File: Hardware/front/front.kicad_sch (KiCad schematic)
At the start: 17 parts, among them J101 Conn_02x10_Odd_Even, J102 Conn_02x08_Odd_Even, U101 XRA1203, U102 AT24CS32-SSHM, U103 PCA9955B

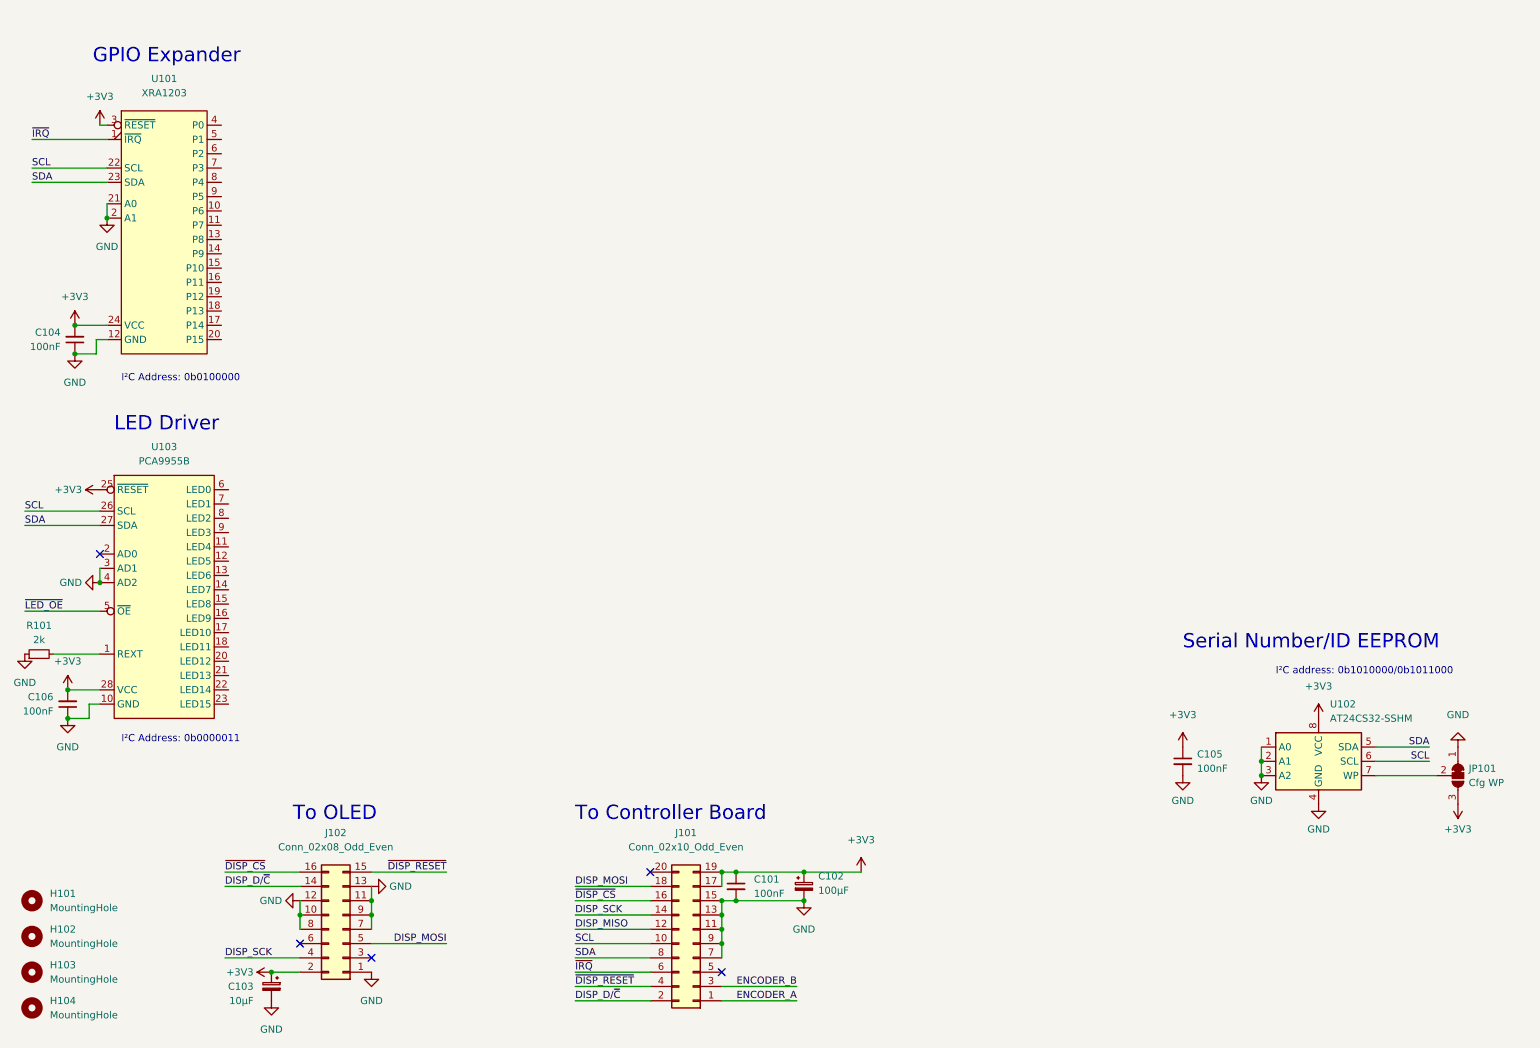
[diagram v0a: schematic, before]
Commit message: Finished front panel board
- Added all the switches/encoders required for the front panel, as well
  as the indicators. They are in (roughly? hopefully lol) the right
  places for the current front panel design.

  The PCB shall be mounted on 4x 8mm standoffs with M2 screws.
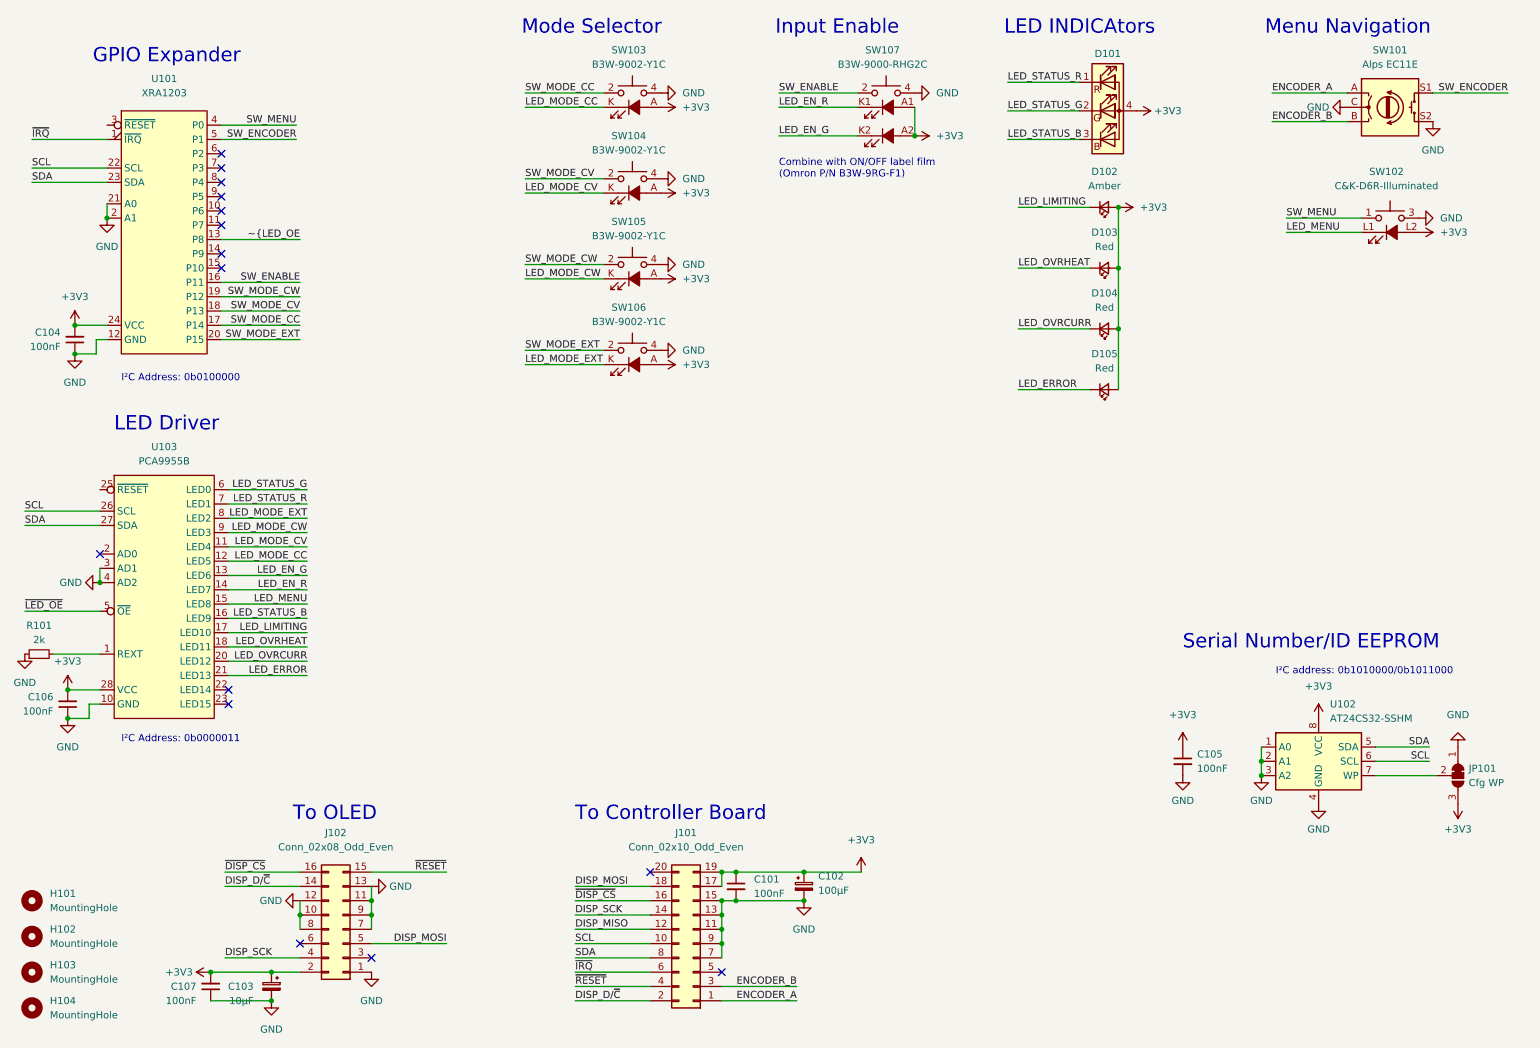
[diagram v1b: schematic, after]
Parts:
- added C107: 100nF, Capacitor_SMD:C_0805_2012Metric_Pad1.18x1.45mm_HandSolder, symbol Device:C_Small
- added D101: LED_RGBA, LED_SMD:LED_RGB_1210, symbol Device:LED_RGBA
- added D102: Amber, LED_SMD:LED_1206_3216Metric_Pad1.42x1.75mm_HandSolder, symbol Device:LED_Small
- added D103, D104, D105: Red, LED_SMD:LED_1206_3216Metric_Pad1.42x1.75mm_HandSolder, symbol Device:LED_Small
- added SW101: Alps EC11E, Rotary_Encoder:RotaryEncoder_Alps_EC11E-Switch_Vertical_H20mm, symbol Device:RotaryEncoder_Switch
- added SW102: C&K-D6R-Illuminated, programmable-load:C&K-D6R-LED, symbol programmable-load:C&K-D6R-Illuminated
- added SW103, SW104, SW105, SW106: B3W-9002-Y1C, programmable-load:Omron-B3W-90XX-X1X, symbol programmable-load:B3W-900X-X1X
- added SW107: B3W-9000-RHG2C, programmable-load:Omron-B3W-90XX-X2X, symbol programmable-load:B3W-900X-X2X
- H101, H102, H103, H104, JP101: now left out of the parts list
- J101: MPN 20021221-00020C1LF -> 20021221-00020C1LF, 20021121-00020C1LF
- J102: footprint Connector_PinHeader_2.54mm:PinHeader_2x08_P2.54mm_Vertical -> Connector_PinHeader_2.54mm:PinHeader_2x08_P2.54mm_Vertical_SMD; MPN (none) -> 10129383-916001ALF
- U101: MPN (none) -> XRA1203IG24TR-F
- U102: MPN (none) -> AT24CS32-SSHM
- U103: MPN (none) -> PCA9955BTWJ
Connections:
- net +3V3: now also C107.2, D101.4 (A), D102.2 (A), D103.2 (A), D104.2 (A), D105.2 (A), SW102.L2, SW103.A, SW104.A, SW105.A, SW106.A, SW107.A1, SW107.A2; no longer U101.3 (~{RESET}), U103.25 (~{RESET})
- net ENCODER_A: now also SW101.A
- net ENCODER_B: now also SW101.B
- net GND: now also C107.1, SW101.C, SW101.S2, SW102.3 (2), SW102.4 (2), SW103.3, SW103.4, SW104.3, SW104.4, SW105.3, SW105.4, SW106.3, SW106.4, SW107.3, SW107.4
- net ~{LED_OE: now reaches U101.13 (P8)
- net SW_ENABLE: now reaches U101.16 (P11)
- net SW_ENABLE: now also SW107.1, SW107.2
- net SW_MODE_CC: now reaches U101.17 (P14)
- net SW_MODE_CC: now also SW103.1, SW103.2
- net SW_MODE_CV: now reaches U101.18 (P13)
- net SW_MODE_CV: now also SW104.1, SW104.2
- net SW_MODE_CW: now reaches U101.19 (P12)
- net SW_MODE_CW: now also SW105.1, SW105.2
- net SW_MODE_EXT: now reaches U101.20 (P15)
- net SW_MODE_EXT: now also SW106.1, SW106.2
- net SW_MENU: now reaches U101.4 (P0)
- net SW_MENU: now also SW102.1, SW102.2 (1)
- net SW_ENCODER: now reaches U101.5 (P1)
- net SW_ENCODER: now also SW101.S1
- net LED_MODE_CV: now reaches U103.11 (LED4)
- net LED_MODE_CV: now also SW104.K
- net LED_MODE_CC: now reaches U103.12 (LED5)
- net LED_MODE_CC: now also SW103.K
- net LED_EN_G: now reaches U103.13 (LED6)
- net LED_EN_G: now also SW107.K2 (K)
- net LED_EN_R: now reaches U103.14 (LED7)
- net LED_EN_R: now also SW107.K1 (K)
- net LED_MENU: now reaches U103.15 (LED8)
- net LED_MENU: now also SW102.L1
- net LED_STATUS_B: now reaches U103.16 (LED9)
- net LED_STATUS_B: now also D101.3 (BK)
- net LED_LIMITING: now reaches U103.17 (LED10)
- net LED_LIMITING: now also D102.1 (K)
- net LED_OVRHEAT: now reaches U103.18 (LED11)
- net LED_OVRHEAT: now also D103.1 (K)
- net LED_OVRCURR: now reaches U103.20 (LED12)
- net LED_OVRCURR: now also D104.1 (K)
- net LED_ERROR: now reaches U103.21 (LED13)
- net LED_ERROR: now also D105.1 (K)
- net LED_STATUS_G: now reaches U103.6 (LED0)
- net LED_STATUS_G: now also D101.2 (GK)
- net LED_STATUS_R: now reaches U103.7 (LED1)
- net LED_STATUS_R: now also D101.1 (RK)
- net LED_MODE_EXT: now reaches U103.8 (LED2)
- net LED_MODE_EXT: now also SW106.K
- net LED_MODE_CW: now reaches U103.9 (LED3)
- net LED_MODE_CW: now also SW105.K
- net ~{DISP_RESET} renamed ~{RESET}
- no-connect marks 5 -> 15
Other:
- note added: "Combine with ON/OFF label film (Omron P/N B3W-9RG-F1)"
- note added: "Input Enable"
- note added: "LED INDICAtors"
- note added: "Menu Navigation"
- note added: "Mode Selector"

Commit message: Front panel layout tweaks
- Made space for a ~38mm diameter knob on the rotary encoder, by moving
  the indicators and menu button somewhat.
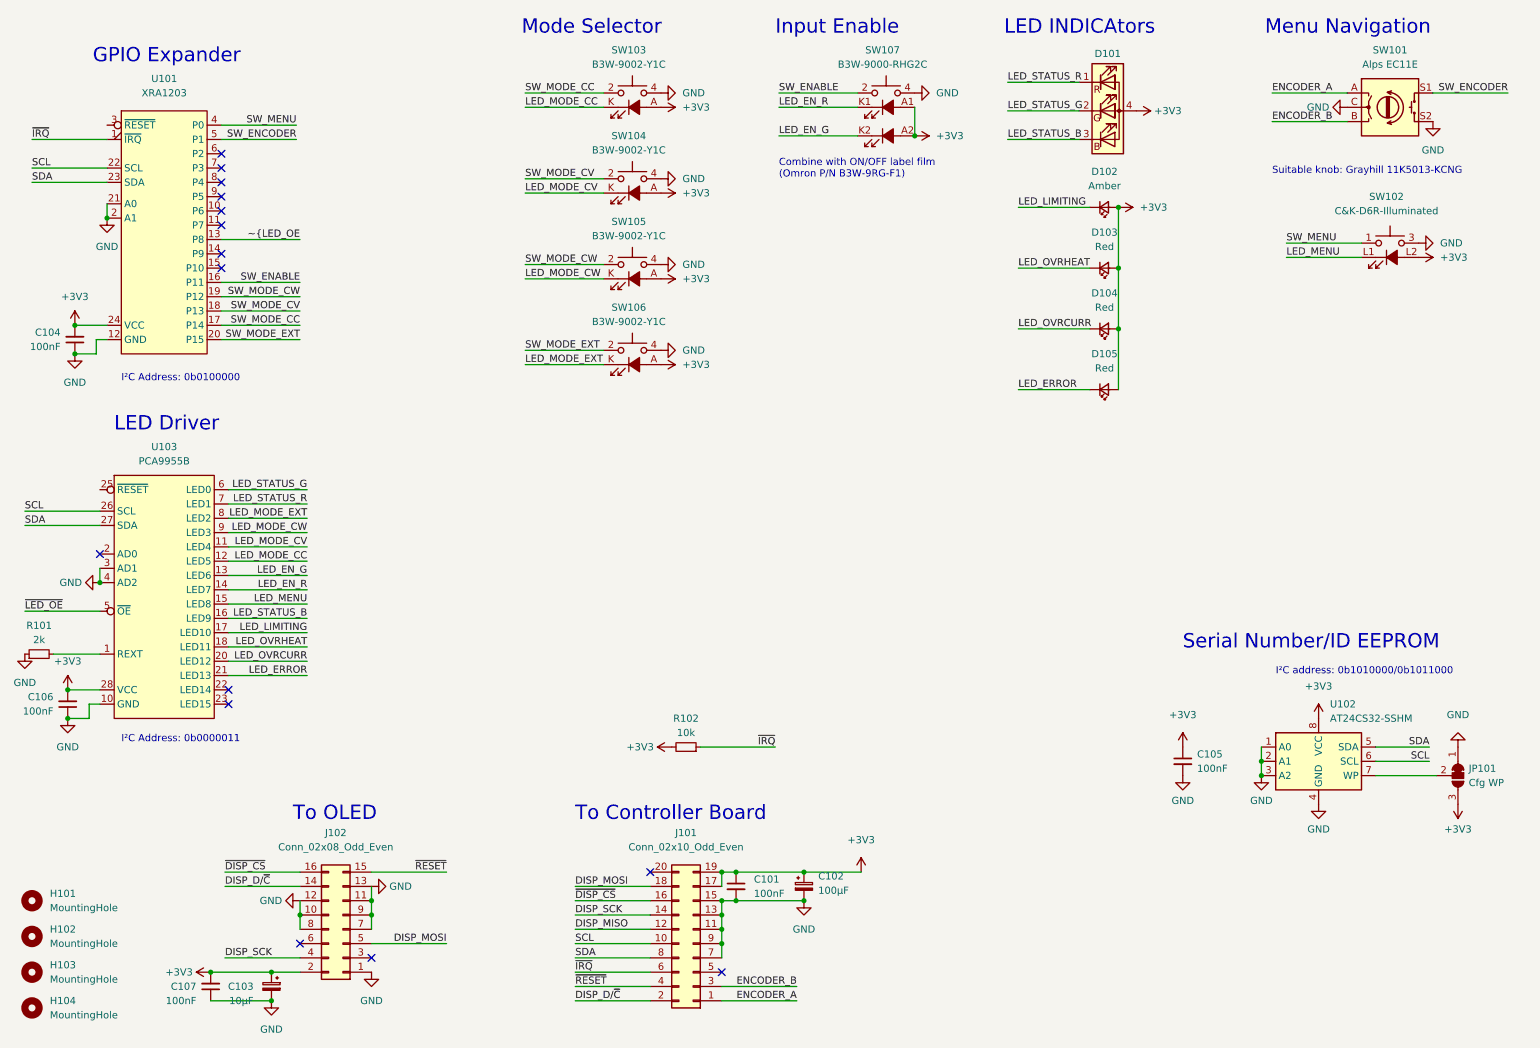
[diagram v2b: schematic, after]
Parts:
- added R102: 10k, Resistor_SMD:R_0805_2012Metric_Pad1.20x1.40mm_HandSolder, symbol Device:R_Small
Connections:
- net +3V3: now also R102.2
- net ~{IRQ}: now also R102.1
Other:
- note added: "Suitable knob: Grayhill 11K5013-KCNG"
- moved on the sheet: SW102
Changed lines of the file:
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@@
+    (stroke (width 0) (type default) (color 0 0 0 0))
+  )
+  (wire (pts (xy 151.13 144.145) (xy 137.795 144.145))
     (stroke (width 0) (type default) (color 0 0 0 0))
   )
@@
     (stroke (width 0) (type default) (color 0 0 0 0))
   )
-  (wire (pts (xy 255.27 52.705) (xy 241.935 52.705))
+  (wire (pts (xy 255.27 57.15) (xy 241.935 57.15))
     (stroke (width 0) (type default) (color 0 0 0 0))
   )
@@
     (stroke (width 0) (type default) (color 0 0 0 0))
   )
-  (wire (pts (xy 241.935 50.165) (xy 255.27 50.165))
+  (wire (pts (xy 241.935 54.61) (xy 255.27 54.61))
     (stroke (width 0) (type default) (color 0 0 0 0))
   )
@@
     (effects (font (size 2.54 2.54)) (justify left bottom))
   )
+  (text "Suitable knob: Grayhill 11K5013-KCNG" (at 239.395 42.545 0)
+    (effects (font (size 1.27 1.27)) (justify left bottom))
+  )
   (text "LED INDICAtors" (at 191.77 17.78 0)
     (effects (font (size 2.54 2.54)) (justify left bottom))
@@
     (effects (font (size 1.27 1.27)) (justify left bottom))
   )
-  (label "LED_MENU" (at 241.935 52.705 0)
+  (label "LED_MENU" (at 241.935 57.15 0)
     (effects (font (size 1.27 1.27)) (justify left bottom))
   )
@@
     (effects (font (size 1.27 1.27)) (justify left bottom))
   )
+  (label "~{IRQ}" (at 151.13 144.145 180)
+    (effects (font (size 1.27 1.27)) (justify right bottom))
+  )
   (label "SCL" (at 17.78 102.235 0)
     (effects (font (size 1.27 1.27)) (justify left bottom))
@@
     (effects (font (size 1.27 1.27)) (justify right bottom))
   )
-  (label "SW_MENU" (at 241.935 50.165 0)
+  (label "SW_MENU" (at 241.935 54.61 0)
     (effects (font (size 1.27 1.27)) (justify left bottom))
   )
@@
     (pin "1")
   )
-  (symbol (lib_id "power:GND") (at 265.43 50.165 90) (unit 1)
-    (in_bom yes) (on_board yes) (fields_autoplaced)
-    (property "Reference" "#PWR0126" (id 0) (at 271.78 50.165 0)
-      (effects (font (size 1.27 1.27)) hide)
-    )
-    (property "Value" "GND" (id 1) (at 269.24 50.1649 90)
+  (symbol (lib_id "power:GND") (at 265.43 54.61 90) (unit 1)
+    (in_bom yes) (on_board yes) (fields_autoplaced)
+    (property "Reference" "#PWR0126" (id 0) (at 271.78 54.61 0)
+      (effects (font (size 1.27 1.27)) hide)
+    )
+    (property "Value" "GND" (id 1) (at 269.24 54.6099 90)
       (effects (font (size 1.27 1.27)) (justify right))
     )
-    (property "Footprint" "" (id 2) (at 265.43 50.165 0)
-      (effects (font (size 1.27 1.27)) hide)
-    )
-    (property "Datasheet" "" (id 3) (at 265.43 50.165 0)
+    (property "Footprint" "" (id 2) (at 265.43 54.61 0)
+      (effects (font (size 1.27 1.27)) hide)
+    )
+    (property "Datasheet" "" (id 3) (at 265.43 54.61 0)
       (effects (font (size 1.27 1.27)) hide)
     )
@@
     (pin "1")
   )
+  (symbol (lib_id "power:+3V3") (at 132.715 144.145 90) (unit 1)
+    (in_bom yes) (on_board yes) (fields_autoplaced)
+    (property "Reference" "#PWR0110" (id 0) (at 136.525 144.145 0)
+      (effects (font (size 1.27 1.27)) hide)
+    )
+    (property "Value" "+3V3" (id 1) (at 129.54 144.1449 90)
+      (effects (font (size 1.27 1.27)) (justify left))
+    )
+    (property "Footprint" "" (id 2) (at 132.715 144.145 0)
+      (effects (font (size 1.27 1.27)) hide)
+    )
+    (property "Datasheet" "" (id 3) (at 132.715 144.145 0)
+      (effects (font (size 1.27 1.27)) hide)
+    )
+    (pin "1")
+  )
   (symbol (lib_name "B3W-900X-X1X_2") (lib_id "programmable-load:B3W-900X-X1X") (at 125.73 45.72 0) (unit 1)
     (in_bom yes) (on_board yes)
@@
     (pin "1")
   )
-  (symbol (lib_id "programmable-load:C&K-D6R-Illuminated") (at 260.35 46.355 0) (unit 1)
-    (in_bom yes) (on_board yes) (fields_autoplaced)
-    (property "Reference" "SW102" (id 0) (at 259.715 41.91 0))
-    (property "Value" "C&K-D6R-Illuminated" (id 1) (at 259.715 44.45 0))
-    (property "Footprint" "programmable-load:C&K-D6R-LED" (id 2) (at 260.35 46.355 0)
-      (effects (font (size 1.27 1.27)) hide)
-    )
-    (property "Datasheet" "https://www.mouser.com/datasheet/2/60/d6-1382571.pdf" (id 3) (at 260.35 46.355 0)
-      (effects (font (size 1.27 1.27)) hide)
-    )
-    (property "MPN" "D6RLRD F1 LFS" (id 4) (at 260.35 46.355 0)
+  (symbol (lib_id "programmable-load:C&K-D6R-Illuminated") (at 260.35 50.8 0) (unit 1)
+    (in_bom yes) (on_board yes) (fields_autoplaced)
+    (property "Reference" "SW102" (id 0) (at 259.715 46.355 0))
+    (property "Value" "C&K-D6R-Illuminated" (id 1) (at 259.715 48.895 0))
+    (property "Footprint" "programmable-load:C&K-D6R-LED" (id 2) (at 260.35 50.8 0)
+      (effects (font (size 1.27 1.27)) hide)
+    )
+    (property "Datasheet" "https://www.mouser.com/datasheet/2/60/d6-1382571.pdf" (id 3) (at 260.35 50.8 0)
+      (effects (font (size 1.27 1.27)) hide)
+    )
+    (property "MPN" "D6RLRD F1 LFS" (id 4) (at 260.35 50.8 0)
       (effects (font (size 1.27 1.27)) hide)
     )
@@
     )
   )
+  (symbol (lib_id "Device:R_Small") (at 135.255 144.145 270) (mirror x) (unit 1)
+    (in_bom yes) (on_board yes)
+    (property "Reference" "R102" (id 0) (at 135.255 139.065 90))
+    (property "Value" "10k" (id 1) (at 135.255 141.605 90))
+    (property "Footprint" "Resistor_SMD:R_0805_2012Metric_Pad1.20x1.40mm_HandSolder" (id 2) (at 135.255 144.145 0)
+      (effects (font (size 1.27 1.27)) hide)
+    )
+    (property "Datasheet" "~" (id 3) (at 135.255 144.145 0)
+      (effects (font (size 1.27 1.27)) hide)
+    )
+    (property "MPN" "RMC1/10-103JTP" (id 4) (at 135.255 144.145 90)
+      (effects (font (size 1.27 1.27)) hide)
+    )
+    (pin "1")
+    (pin "2")
+  )
   (symbol (lib_id "Device:C_Small") (at 223.52 146.685 0) (unit 1)
     (in_bom yes) (on_board yes) (fields_autoplaced)
@@
     (pin "K")
   )
-  (symbol (lib_id "power:+3V3") (at 265.43 52.705 270) (unit 1)
-    (in_bom yes) (on_board yes) (fields_autoplaced)
-    (property "Reference" "#PWR0128" (id 0) (at 261.62 52.705 0)
-      (effects (font (size 1.27 1.27)) hide)
-    )
-    (property "Value" "+3V3" (id 1) (at 269.24 52.7049 90)
-      (effects (font (size 1.27 1.27)) (justify left))
-    )
-    (property "Footprint" "" (id 2) (at 265.43 52.705 0)
-      (effects (font (size 1.27 1.27)) hide)
-    )
-    (property "Datasheet" "" (id 3) (at 265.43 52.705 0)
+  (symbol (lib_id "power:+3V3") (at 265.43 57.15 270) (unit 1)
+    (in_bom yes) (on_board yes) (fields_autoplaced)
+    (property "Reference" "#PWR0128" (id 0) (at 261.62 57.15 0)
+      (effects (font (size 1.27 1.27)) hide)
+    )
+    (property "Value" "+3V3" (id 1) (at 269.24 57.1499 90)
+      (effects (font (size 1.27 1.27)) (justify left))
+    )
+    (property "Footprint" "" (id 2) (at 265.43 57.15 0)
+      (effects (font (size 1.27 1.27)) hide)
+    )
+    (property "Datasheet" "" (id 3) (at 265.43 57.15 0)
       (effects (font (size 1.27 1.27)) hide)
     )
@@
       (reference "#PWR0109") (unit 1) (value "GND") (footprint "")
     )
+    (path "/83a98620-70cb-42d9-a59c-bb49b2558f09"
+      (reference "#PWR0110") (unit 1) (value "+3V3") (footprint "")
+    )
     (path "/a8b8f491-e7f6-4bea-b492-8a27822d6714"
       (reference "#PWR0111") (unit 1) (value "GND") (footprint "")
@@
       (reference "R101") (unit 1) (value "2k") (footprint "Resistor_SMD:R_0805_2012Metric_Pad1.20x1.40mm_HandSolder")
     )
+    (path "/e76f0c23-3dcd-483a-a6f9-721673d8aaf1"
+      (reference "R102") (unit 1) (value "10k") (footprint "Resistor_SMD:R_0805_2012Metric_Pad1.20x1.40mm_HandSolder")
+    )
     (path "/99deab52-0fbc-4866-8276-198c86debfa9"
